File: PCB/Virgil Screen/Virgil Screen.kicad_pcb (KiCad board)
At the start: 2 copper layers, 20 x 72 mm, 13 parts, among them J3 SFV20R-2STE1HLF, Q1 SS8550, U1 XIAO-RP2350-SMD, U2 ZJY114TC-IF03-HSD, U4 SN74LVC1T45DBV

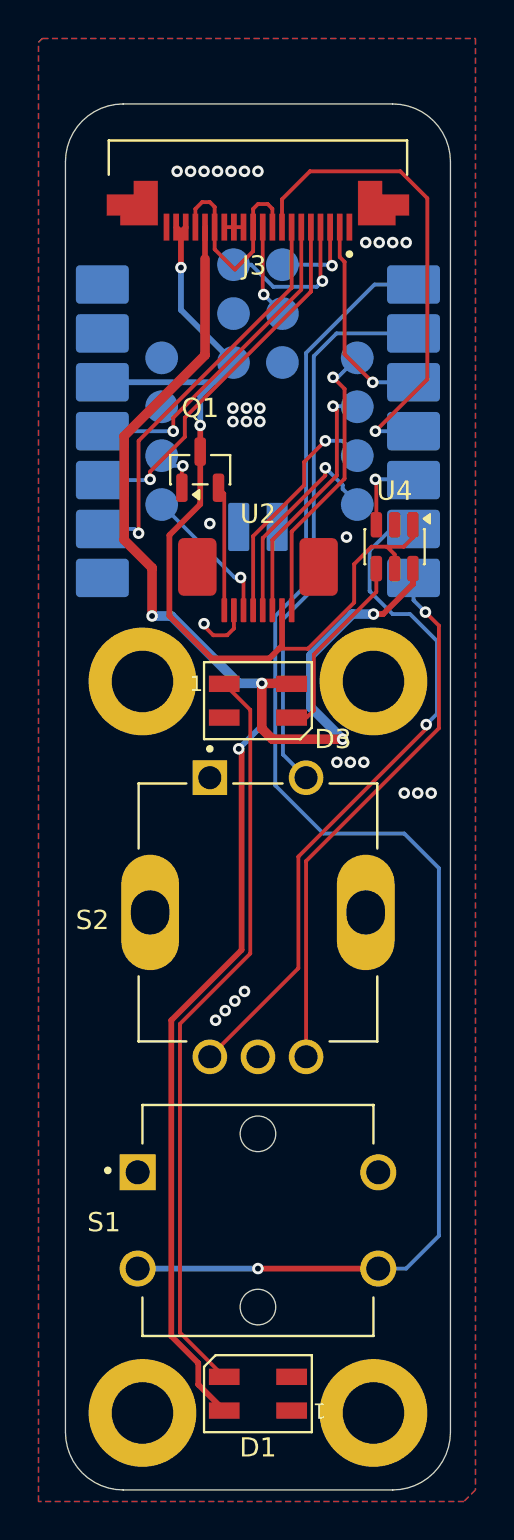
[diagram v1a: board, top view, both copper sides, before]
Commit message: Updated PCBs to use raw rp2040s
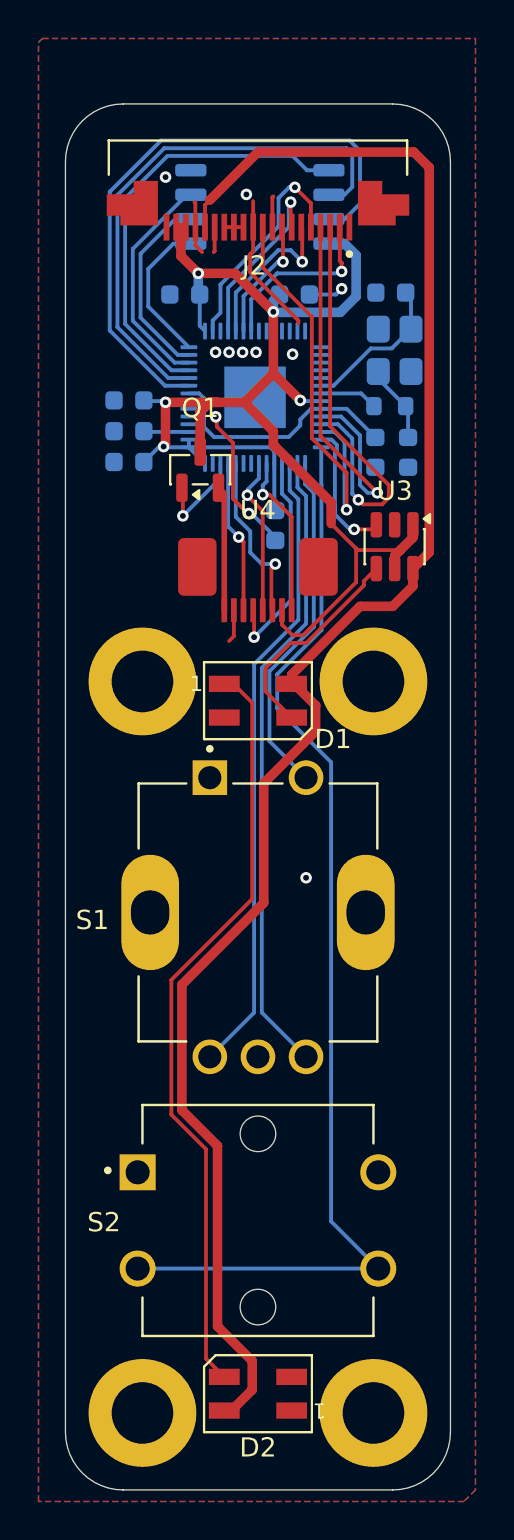
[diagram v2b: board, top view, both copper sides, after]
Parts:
- added C1: 22pF, Capacitor_SMD:C_0603_1608Metric, B.Cu at (131.9, 74.8)
- added C10: 100nF, Capacitor_SMD:C_0603_1608Metric, B.Cu at (131.1, 83.1)
- added C2: 22pF, Capacitor_SMD:C_0603_1608Metric, B.Cu at (132.8, 83.1)
- added C4: 100nF, Capacitor_SMD:C_0603_1608Metric, B.Cu at (126.9, 74.9)
- added C5: 100nF, Capacitor_SMD:C_0603_1608Metric, B.Cu at (125.9, 86.9)
- added C6: 100nF, Capacitor_SMD:C_0603_1608Metric, B.Cu at (121.2, 74.9)
- added C7: 100nF, Capacitor_SMD:C_0603_1608Metric, B.Cu at (118.3, 80.4)
- added C8: 100nF, Capacitor_SMD:C_0603_1608Metric, B.Cu at (118.3, 83.6)
- added C9: 100nF, Capacitor_SMD:C_0603_1608Metric, B.Cu at (118.3, 82.0)
- added R1: 1kΩ, Resistor_SMD:R_0603_1608Metric, B.Cu at (131.8, 80.7)
- added U2: RP2040, Package_DFN_QFN:QFN-56-1EP_7x7mm_P0.4mm_EP3.2x3.2mm, B.Cu at (124.8, 80.2)
- added Y1: Crystal_GND24, Crystal:Crystal_SMD_Abracon_ABM8G-4Pin_3.2x2.5mm, B.Cu at (132.1, 77.8)
- U1: value XIAO-RP2350-SMD -> W25Q16JVSS; footprint Snapeda:XIAO-RP2350-SMD -> Package_SO:SOIC-8_5.3x5.3mm_P1.27mm
- moved U1 11.7 mm to (125.1, 70.3), turned to 0 degrees
- renumbered D3 to D1, D1 to D2, J3 to J2, S2 to S1, S1 to S2, U4 to U3, U2 to U4
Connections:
- U1 pad 1: /Button -> Net-(U1-~{CS})
- U1 pad 2: /KnobButton -> /QSPI_SD1
- U1 pad 3: /~{INT} -> /QSPI_SD2
- U1 pad 4: /~{FlashCS} -> GND
- U1 pad 5: /Neopixel -> /QSPI_SD0
- U1 pad 6: /CHANNEL_A -> /QSPI_SCLK
- U1 pad 7: /CHANNEL_B -> /QSPI_SD3
- U1 pad 8: unconnected-(U1-GPIO1_D7_RX0-Pad8) -> +3.3V
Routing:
- net /QSPI_SD3: track 0.00 -> 31.5 mm
- net /QSPI_SCLK: track 0.00 -> 28.1 mm
- net +3.3V: track 51.8 -> 77.0 mm, vias 2 -> 5
- net /QSPI_SD0: track 0.00 -> 22.6 mm
- net /~{FlashCS}: track 25.4 -> 6.35 mm
- net /SWDIO: track 4.64 -> 22.4 mm
- net /Button: track 75.9 -> 58.3 mm, vias 1 -> 0
- net /~{RST}: track 4.91 -> 21.5 mm
- net +1V1: track 0.00 -> 16.1 mm
- net /SWCLK: track 8.06 -> 21.1 mm
- net /CLK: track 21.2 -> 9.30 mm
- net /QSPI_SD2: track 0.00 -> 11.5 mm
- net /KnobButton: track 28.7 -> 18.3 mm
- net /QSPI_SD1: track 0.00 -> 9.99 mm
- net GND: track 14.6 -> 24.3 mm, vias 30 -> 11
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
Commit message: Finished PCBs
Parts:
- C1, C2: value 22pF -> 15pF
- J2: value SFV20R-2STE1HLF -> AFC07-S20FCC-00
- U4: value ZJY114TC-IF03-HSD -> AFC07-S08ECC-00
- Y1: value Crystal_GND24 -> ABM8-272-T3

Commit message: Started code, commiting before adding submodules
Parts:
- J2: footprint Snapeda:AMPHENOL_SFV20R-2STE1HLF -> Snapeda:JUSHUO AFC07-S20FCC-00
- moved J2 2.40 mm to (125.0, 71.4)
